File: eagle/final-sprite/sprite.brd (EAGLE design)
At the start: 35 x 35 mm, 40 parts

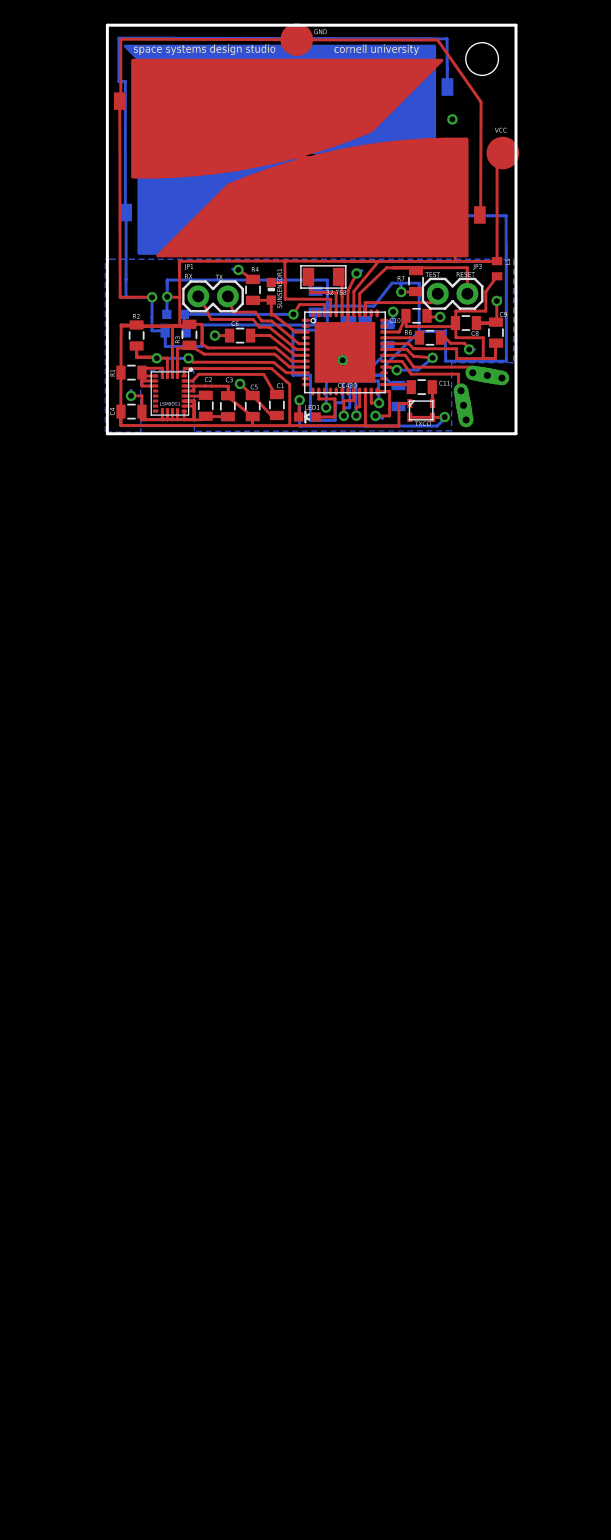
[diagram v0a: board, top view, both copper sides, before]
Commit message: merged final-sprite changes into master branch
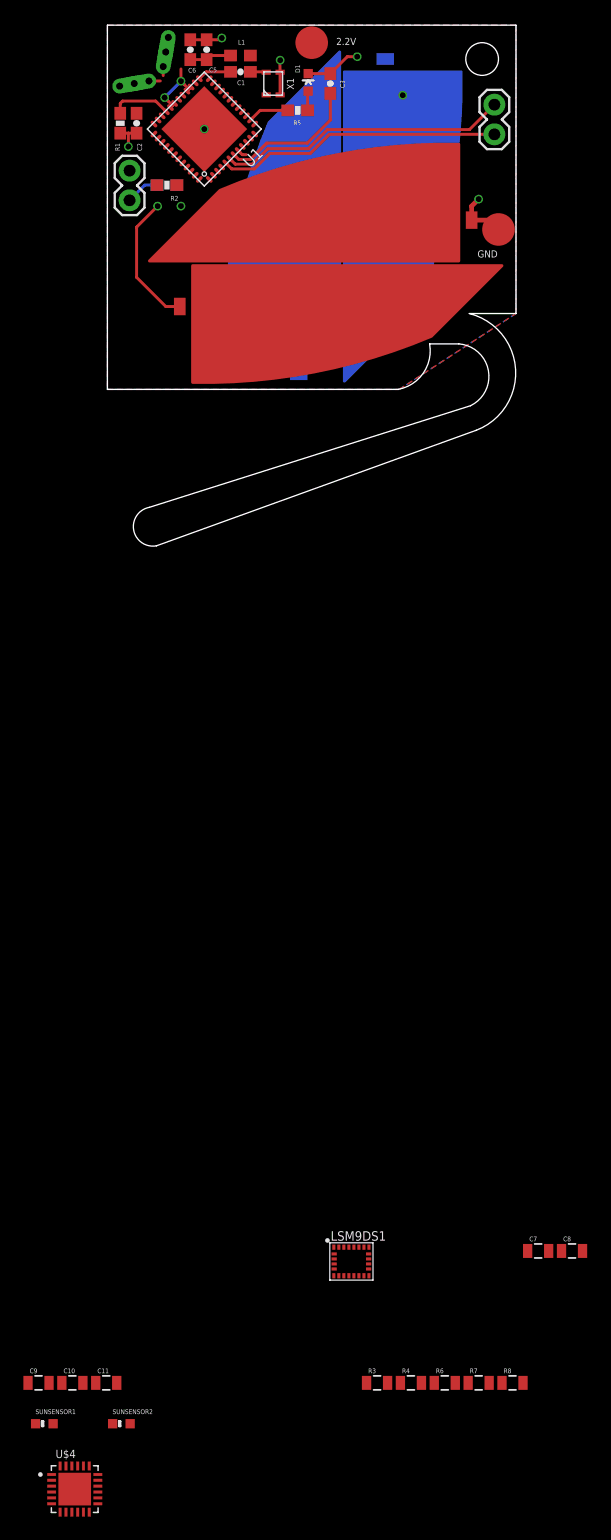
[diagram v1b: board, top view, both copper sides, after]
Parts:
- removed 32KHZ: SPRITECRYSTALSPRITECRYSTAL, SpriteCrystal:SPRITECRYSTAL
- removed ANTENNA1, ANTENNA2: ANTENNA, SpriteAntenna:ANTENNA
- removed C12: 10uF, SparkFun:0805
- removed CC430: CC430F513X---RGZ48, TI_MSP430_v16:RGZ48
- removed GNDPIN, VCCPIN: SPRITE_PIN, SpritePin:SPRITE_PIN
- removed H-BRIDGE: LV8417CS, lv8417cs:LV8417CS
- removed JP1: (no value), SparkFun:1X02
- removed LED1: (no value), SparkFun:LED-0603
- removed RECTIFIER: NSR1030QMUTAG, NSR1030QMUTAG:NSR1030QMUTAG
- removed TRISOL1, TRISOL2, TRISOL3, TRISOL4: TRISOLX-WING, TriSolX_QzQube:TRISOLX-T01
- removed TXCO: (no value), SpriteTCXO:TXC_7Z
- added ANT-N, ANT-P: ANTENNA, SpriteAntenna:ANTENNA
- added D1: (no value), SparkFun:LED-0603
- added JP2: (no value), SparkFun:1X02
- added P1, P2: SPRITE_PIN, SpritePin:SPRITE_PIN
- added S1, S2, S3, S4: TRISOLX-WING, TriSolX_QzQube:TRISOLX-T01
- added U$1: UMAC, UMAC:UMAC
- added U$4: ADP5092, STAC:QFN50P400X400X100-25N
- added U1: CC430F5137, TI_MSP430_v16:RGZ48
- added X1: TCXO_7Z, SpriteTCXO:TXC_7Z
- C1: value 0.1uF -> 10 nF; device SparkFun:0805 -> SparkFun:0603-CAP
- C10: value 470nF -> 0.1uF
- C11: value 10nF -> 10uF
- C2: value 10nF -> 470nF; device SparkFun:0805 -> SparkFun:0603-CAP
- C3: value 0.1uF -> 470nF; device SparkFun:0805 -> SparkFun:0603-CAP
- C4: value 0.1uF -> 2.2nF; device SparkFun:0805 -> SparkFun:0603-CAP
- C5: value 10uF -> 10nF; device SparkFun:0805 -> SparkFun:0603-CAP
- C6: value 470nF -> 100nF; device SparkFun:0805 -> SparkFun:0603-CAP
- C7: value 10uF -> 0.1uF
- L1: value 12nH -> 12 nH; device SparkFun:C0402 -> SparkFun:0603
- R1: value 10K -> 56K; device SparkFun:0805 -> SparkFun:0603-RES
- R2: value 10K -> 47K; device SparkFun:0805 -> SparkFun:0603-RES
- R5: value 10K -> 270R; device SparkFun:0805 -> SparkFun:0603-RES
- R6, R7: value 56K -> 10K
- R8: value 1K -> 10K
- moved SUNSENSOR1 98.9 mm to (-5.40, -84.8), turned to 0 degrees
- moved C9 98.1 mm to (-5.90, -81.3), turned to 0 degrees
- moved C10 96.0 mm to (-3.00, -81.3)
- moved SUNSENSOR2 95.1 mm to (1.20, -84.8), flipped to the top, turned to 0 degrees
- moved R4 94.6 mm to (26.0, -81.3), turned to 0 degrees
- moved R7 94.5 mm to (31.8, -81.3), turned to 0 degrees
- moved R3 91.2 mm to (23.1, -81.3), turned to 0 degrees
- moved R8 90.4 mm to (34.7, -81.3), flipped to the top, turned to 0 degrees
- moved R6 89.5 mm to (28.9, -81.3), turned to 0 degrees
- moved C11 89.5 mm to (-0.10, -81.3)
- moved C7 83.5 mm to (36.9, -70.0), flipped to the top, turned to 0 degrees
- moved C8 80.0 mm to (39.8, -70.0)
- moved LSM9DS1 76.0 mm to (20.9, -70.9), turned to 0 degrees
- moved C5 30.8 mm to (8.50, 32.9)
- moved C3 29.0 mm to (19.1, 30.0), turned to 90 degrees
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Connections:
- removed net #RST/SBWTDIO: CC430.40, JP3.1, R7.2
- removed net ANT1: ANTENNA1.IN1, ANTENNA1.IN2, ANTENNA1.IN3, CC430.29
- removed net ANT2: ANTENNA2.IN1, ANTENNA2.IN2, ANTENNA2.IN3, CC430.30
- removed net COIL1: H-BRIDGE.OUT1, R8.1, RECTIFIER.PIN1
- removed net GUARD: C10.1, C8.1, C9.1, CC430.27, CC430.28, CC430.31, CC430.32, CC430.34, L1.2
- removed net LOADLINE: H-BRIDGE.OUT2, R8.2, RECTIFIER.PIN3
- removed net N$8: 32KHZ.PIN1, CC430.43
- removed net P1.0: CC430.13
- removed net P1.1: CC430.12
- removed net P1.2: CC430.11
- removed net P1.7: CC430.4
- removed net P2.1/A1: CC430.2
- removed net P2.2/A2: CC430.1
- removed net P2.2/A4: CC430.47
- removed net P2.3/A3: CC430.48
- removed net P2.6: CC430.24
- removed net P2.7: CC430.23, H-BRIDGE.IN2
- removed net P3.0: CC430.21, H-BRIDGE.IN1
- removed net P3.1: CC430.20, H-BRIDGE.ENA
- removed net P3.2: CC430.19
- removed net P3.3: CC430.18
- removed net P3.4: CC430.17
- removed net P3.5: CC430.16
- removed net P3.6: CC430.15
- removed net P3.7: CC430.14, LED1.A
- removed net R_BIAS: CC430.33, R6.2
- removed net TCK_PJ.3: CC430.38
- removed net TDI_PJ.1: CC430.36
- removed net TDO_PJ.0: CC430.35
- removed net TEST/SBWTCK: CC430.39, JP3.2
- removed net TMS_PJ.2: CC430.37
- removed net VCORE: C6.2, CC430.7
- new net N$11: D1.A, R5.1
- new net N$12: C1.2, X1.OUT
- new net N$6: C8.1, LSM9DS1.21
- new net PGOOD: U$4.19
- new net REGGOOD: U$4.11
- new net RF_N: ANT-N.IN1, ANT-N.IN2, ANT-N.IN3, U1.30
- new net RF_P: ANT-P.IN1, ANT-P.IN2, ANT-P.IN3, U1.29
- new net RST: C4.2, JP2.1, R2.1, U1.40
- new net TST: JP2.2, U1.39
- new net VBAT: U$1.V+, U$4.17
- new net VCCA: C5.1, C6.1, L1.2, U1.27, U1.28, U1.31, U1.32
- new net VCCINT: S1.P$2, S2.P$2, S3.P$2, S4.P$2
- new net VCCIO: U$4.14, U$4.15
- net GND: now also C11.2, C4.1, C6.2, C7.2, D1.C, P2.PIN, R1.2, R7.1, R8.1, S1.P$3, S2.P$3, S3.P$3, S4.P$3, U$1.V-, U$4.12, U$4.25, U$4.7, U1.42, U1.TP, X1.GND1, X1.GND2; no longer C1.2, C12.1, C4.2, C6.1, C7.1, CC430.42, CC430.TP, GNDPIN.PIN, H-BRIDGE.PGND, H-BRIDGE.SGND, LED1.C, R4.1, R5.1, R6.1, RECTIFIER.GND, TRISOL1.P$3, TRISOL2.P$3, TRISOL3.P$3, TRISOL4.P$3, TXCO.GND1, TXCO.GND2
- net N$1: now also U1.25; no longer LSM9DS1.24
- net N$2: now also R5.2, U1.14; no longer C2.1, LSM9DS1.21
- net N$3: now also U1.33; no longer LSM9DS1.5, LSM9DS1.6, LSM9DS1.7, LSM9DS1.8
- net N$4: now also C3.1, U1.7; no longer C11.1, CC430.25
- net N$5: now also C7.1, LSM9DS1.24; no longer C11.2, TXCO.OUT
- net N$7: now also LSM9DS1.5, LSM9DS1.6, LSM9DS1.7, LSM9DS1.8, R3.1; no longer 32KHZ.PIN2, CC430.44
- net P2.0/A0: now also R7.2; no longer CC430.3, R4.2
- net P2.5/A5: now also R8.2; no longer CC430.46, R5.2
- net SCL: now also R6.1, U1.9; no longer CC430.9, R3.1
- net SDA: now also R4.1, U1.10; no longer CC430.10, R2.1
- net UART_RX: now also JP3.2, U1.6; no longer CC430.6, JP1.2
- net UART_TX: now also JP3.1, U1.5; no longer CC430.5, JP1.1
- net VCC: now also C10.1, C11.1, C2.1, C9.1, P1.PIN, R4.2, R6.2, U$4.16, U1.22, U1.34, U1.41, U1.45, U1.8, X1.VCC; no longer C12.2, C3.1, C4.1, C5.1, C7.2, CC430.22, CC430.41, CC430.45, CC430.8, H-BRIDGE.VCC, H-BRIDGE.VM, R1.2, R7.1, RECTIFIER.VCC, TRISOL1.P$2, TRISOL2.P$2, TRISOL3.P$2, TRISOL4.P$2, TXCO.VCC, VCCPIN.PIN
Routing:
- net COIL1: track 1132.3 -> 0.00 mm, vias 3 -> 0
- net VCC: track 371.4 -> 0.85 mm, vias 2 -> 0
- net GND: track 226.3 -> 29.9 mm, vias 12 -> 6
- net GUARD: track 44.1 -> 0.00 mm, vias 2 -> 0
- net VCCINT: track 0.00 -> 23.3 mm, vias 0 -> 1
- net SDA: track 21.1 -> 0.00 mm, vias 2 -> 0
- net #RST/SBWTDIO: track 16.1 -> 0.00 mm
- net UART_TX: track 8.73 -> 24.5 mm
- net P2.5/A5: track 14.7 -> 0.00 mm, vias 1 -> 0
- net SCL: track 14.6 -> 0.00 mm
- net UART_RX: track 11.6 -> 25.0 mm
- net ANT1: track 11.2 -> 0.00 mm
- net ANT2: track 11.1 -> 0.00 mm
- net VCCA: track 0.00 -> 9.55 mm, vias 0 -> 2
- net N$4: track 2.55 -> 12.1 mm
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- added copper zone on layer 1, net VCC
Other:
- board size 35 x 35 mm -> 35 x 44.6 mm
- board text added: "2.2V"
- board text added: "Sprite v2.6"
- board text removed: "RESET"
- board text removed: "RX"
- board text removed: "TEST"
- board text removed: "TX"
- board text removed: "VCC"
- board text removed: "cornell university"
- board text removed: "space systems design studio"

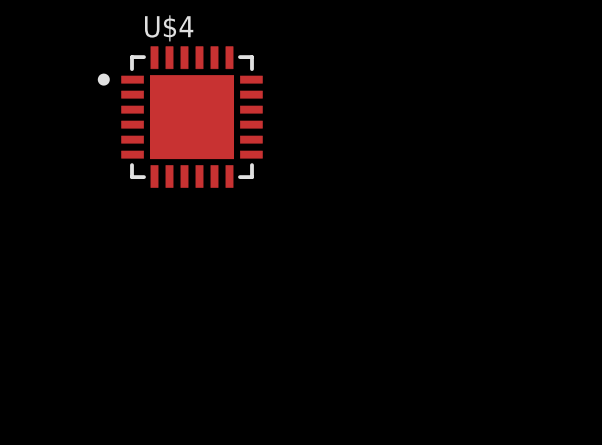
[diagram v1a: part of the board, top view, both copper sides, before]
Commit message: Add DRV8833CRTER
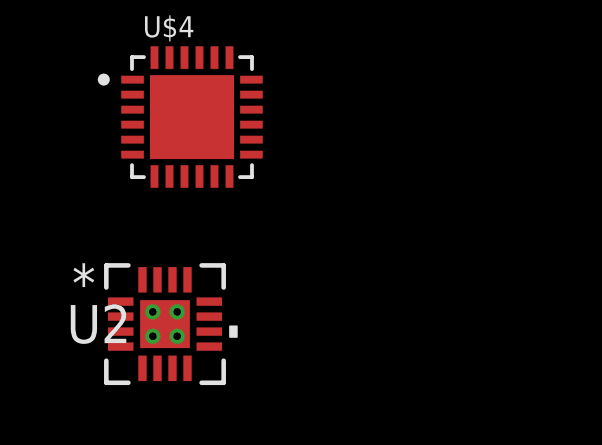
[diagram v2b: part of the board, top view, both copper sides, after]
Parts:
- added U2: DRV8833CRTER, STAC:RTE16_1P66X1P66
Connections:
- new net VM: U2.10
- net GND: now also U2.11
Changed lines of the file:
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@@
 <?xml version="1.0" encoding="utf-8"?>
 <!DOCTYPE eagle SYSTEM "eagle.dtd">
-<eagle version="9.0.1">
+<eagle version="9.0.0">
 <drawing>
 <settings>
@@
 <element name="R8" library="SparkFun" package="0805" value="10K" x="34.7" y="-81.3"/>
 <element name="U$4" library="STAC" package="QFN50P400X400X100-25N" value="ADP5092" x="-2.8" y="-90.4"/>
+<element name="U2" library="STAC" package="RTE16_1P66X1P66" value="DRV8833CRTER" x="-3.7" y="-97.3">
+<attribute name="AUTHOR" value="Ultra-Librarian" x="-3.7" y="-97.3" size="1.778" layer="27" display="off"/>
+<attribute name="CHECKED" value="Kevin Zheng" x="-3.7" y="-97.3" size="1.778" layer="27" display="off"/>
+<attribute name="DIGI-KEY_PN" value="296-40079-1-ND" x="-3.7" y="-97.3" size="1.778" layer="27" display="off"/>
+<attribute name="MANUFACTURER_PART_NUMBER" value="DRV8833CRTER" x="-3.7" y="-97.3" size="1.778" layer="27" display="off"/>
+<attribute name="VENDOR" value="Texas Instruments" x="-3.7" y="-97.3" size="1.778" layer="27" display="off"/>
+</element>
 </elements>
 <signals>
@@
 <contactref element="U$4" pad="12"/>
 <contactref element="U$4" pad="25"/>
-<wire x1="-2.8" y1="-90.4" x2="-4.05" y2="-92.38" width="0" layer="19" extent="1-1"/>
-<wire x1="-1.55" y1="-92.38" x2="-2.8" y2="-90.4" width="0" layer="19" extent="1-1"/>
+<contactref element="U2" pad="11"/>
+<wire x1="-1.55" y1="-92.38" x2="-2.225" y2="-97.05" width="0" layer="19" extent="1-1"/>
+<wire x1="-2.8" y1="-90.4" x2="-1.55" y2="-92.38" width="0" layer="19" extent="1-1"/>
+<wire x1="-4.05" y1="-92.38" x2="-2.8" y2="-90.4" width="0" layer="19" extent="1-1"/>
 <wire x1="-2.1" y1="-81.3" x2="-2.8" y2="-90.4" width="0" layer="19" extent="1-1"/>
 <wire x1="-5" y1="-81.3" x2="-2.1" y2="-81.3" width="0" layer="19" extent="1-1"/>
@@
 <wire x1="-0.82" y1="-90.65" x2="-0.82" y2="-91.15" width="0" layer="19" extent="1-1"/>
 </signal>
+<signal name="VM">
+<contactref element="U2" pad="10"/>
+</signal>
 </signals>

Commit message: Place COIL?_IN? pins
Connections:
- new net COIL1_IN1: U1.20
- new net COIL1_IN2: U1.19
- new net COIL2_IN1: U1.18
- new net COIL2_IN2: U1.17
- new net COIL3_IN1: U1.2
- new net COIL3_IN2: U1.1
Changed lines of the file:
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@@
 <contactref element="U2" pad="10"/>
+</signal>
+<signal name="COIL1_IN1">
+<contactref element="U1" pad="20"/>
+</signal>
+<signal name="COIL1_IN2">
+<contactref element="U1" pad="19"/>
+</signal>
+<signal name="COIL2_IN1">
+<contactref element="U1" pad="18"/>
+</signal>
+<signal name="COIL2_IN2">
+<contactref element="U1" pad="17"/>
+</signal>
+<signal name="COIL3_IN1">
+<contactref element="U1" pad="2"/>
+</signal>
+<signal name="COIL3_IN2">
+<contactref element="U1" pad="1"/>
 </signal>
 </signals>

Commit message: More progress on COIL12
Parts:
- added C12: 10uF, SparkFun:0603-CAP
- added C13: 2.2uF, SparkFun:0603-CAP
- added R10, R9: 270R, SparkFun:0603-RES
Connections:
- removed net VM: U2.10
- new net COIL12_EN: U1.16, U2.15
- new net COIL12_FAULT: U1.13, U2.6
- new net COIL3_EN: U1.48
- new net COIL3_FAULT: U1.12
- new net N$10: R10.2, U2.1
- new net N$8: C13.1, U2.12
- new net N$9: R9.2, U2.4
- net COIL1_IN1: now also U2.14
- net COIL1_IN2: now also U2.13
- net COIL2_IN1: now also U2.7
- net COIL2_IN2: now also U2.8
- net GND: now also C12.2, C13.2, R10.1, R9.1, U2.17
- net VCCIO: now also C12.1, U2.10
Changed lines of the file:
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@@
 <attribute name="VENDOR" value="Texas Instruments" x="-3.7" y="-97.3" size="1.778" layer="27" display="off"/>
 </element>
+<element name="C12" library="SparkFun" package="0603-CAP" value="10uF" x="-4.8" y="-101.6"/>
+<element name="C13" library="SparkFun" package="0603-CAP" value="2.2uF" x="-4.8" y="-104.6"/>
+<element name="R9" library="SparkFun" package="0603-RES" value="270R" x="-4.8" y="-107.6"/>
+<element name="R10" library="SparkFun" package="0603-RES" value="270R" x="-4.8" y="-110.6"/>
 </elements>
 <signals>
@@
 <contactref element="U$4" pad="25"/>
 <contactref element="U2" pad="11"/>
+<contactref element="U2" pad="17"/>
+<contactref element="C12" pad="2"/>
+<contactref element="C13" pad="2"/>
+<contactref element="R9" pad="1"/>
+<contactref element="R10" pad="1"/>
+<wire x1="-5.65" y1="-107.6" x2="-5.65" y2="-110.6" width="0" layer="19" extent="1-1"/>
+<wire x1="-3.95" y1="-104.6" x2="-5.65" y2="-107.6" width="0" layer="19" extent="1-1"/>
+<wire x1="-3.95" y1="-101.6" x2="-3.95" y2="-104.6" width="0" layer="19" extent="1-1"/>
+<wire x1="-3.7" y1="-97.3" x2="-3.95" y2="-101.6" width="0" layer="19" extent="1-1"/>
+<wire x1="-2.225" y1="-97.05" x2="-3.7" y2="-97.3" width="0" layer="19" extent="1-1"/>
 <wire x1="-1.55" y1="-92.38" x2="-2.225" y2="-97.05" width="0" layer="19" extent="1-1"/>
 <wire x1="-2.8" y1="-90.4" x2="-1.55" y2="-92.38" width="0" layer="19" extent="1-1"/>
@@
 <contactref element="U$4" pad="14"/>
 <contactref element="U$4" pad="15"/>
+<contactref element="C12" pad="1"/>
+<contactref element="U2" pad="10"/>
+<wire x1="-2.225" y1="-97.55" x2="-5.65" y2="-101.6" width="0" layer="19" extent="1-1"/>
+<wire x1="-0.82" y1="-91.15" x2="-2.225" y2="-97.55" width="0" layer="19" extent="1-1"/>
 <wire x1="-0.82" y1="-90.65" x2="-0.82" y2="-91.15" width="0" layer="19" extent="1-1"/>
-</signal>
-<signal name="VM">
-<contactref element="U2" pad="10"/>
 </signal>
 <signal name="COIL1_IN1">
 <contactref element="U1" pad="20"/>
+<contactref element="U2" pad="14"/>
+<wire x1="10.138475" y1="28.9991375" x2="-3.4499375" y2="-95.825" width="0" layer="19" extent="1-1"/>
 </signal>
 <signal name="COIL1_IN2">
 <contactref element="U1" pad="19"/>
+<contactref element="U2" pad="13"/>
+<wire x1="10.492028125" y1="28.645584375" x2="-2.9498125" y2="-95.825" width="0" layer="19" extent="1-1"/>
 </signal>
 <signal name="COIL2_IN1">
 <contactref element="U1" pad="18"/>
+<contactref element="U2" pad="7"/>
+<wire x1="10.845584375" y1="28.292028125" x2="-3.4499375" y2="-98.775" width="0" layer="19" extent="1-1"/>
 </signal>
 <signal name="COIL2_IN2">
 <contactref element="U1" pad="17"/>
+<contactref element="U2" pad="8"/>
+<wire x1="11.1991375" y1="27.938475" x2="-2.9498125" y2="-98.775" width="0" layer="19" extent="1-1"/>
 </signal>
 <signal name="COIL3_IN1">
@@
 <contactref element="U1" pad="1"/>
 </signal>
+<signal name="N$8">
+<contactref element="C13" pad="1"/>
+<contactref element="U2" pad="12"/>
+<wire x1="-2.225" y1="-96.55" x2="-5.65" y2="-104.6" width="0" layer="19" extent="1-1"/>
+</signal>
+<signal name="COIL12_EN">
+<contactref element="U1" pad="16"/>
+<contactref element="U2" pad="15"/>
+<wire x1="11.552690625" y1="27.584921875" x2="-3.9500625" y2="-95.825" width="0" layer="19" extent="1-1"/>
+</signal>
+<signal name="COIL3_EN">
+<contactref element="U1" pad="48"/>
+</signal>
+<signal name="COIL12_FAULT">
+<contactref element="U1" pad="13"/>
+<contactref element="U2" pad="6"/>
+<wire x1="12.61335" y1="26.5242625" x2="-3.9500625" y2="-98.775" width="0" layer="19" extent="1-1"/>
+</signal>
+<signal name="COIL3_FAULT">
+<contactref element="U1" pad="12"/>
+</signal>
+<signal name="N$9">
+<contactref element="R9" pad="2"/>
+<contactref element="U2" pad="4"/>
+<wire x1="-5.175" y1="-98.05" x2="-3.95" y2="-107.6" width="0" layer="19" extent="1-1"/>
+</signal>
+<signal name="N$10">
+<contactref element="R10" pad="2"/>
+<contactref element="U2" pad="1"/>
+<wire x1="-5.175" y1="-96.55" x2="-3.95" y2="-110.6" width="0" layer="19" extent="1-1"/>
+</signal>
 </signals>

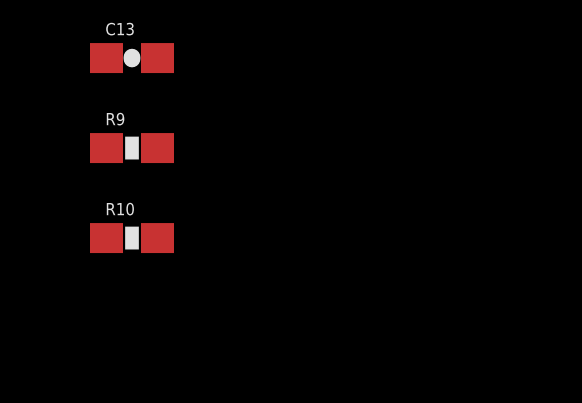
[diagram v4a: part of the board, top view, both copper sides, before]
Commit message: Complete one driver
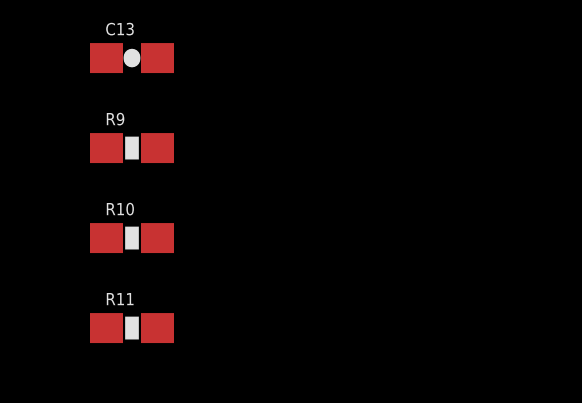
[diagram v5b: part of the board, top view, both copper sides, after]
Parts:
- added R11: 1K, SparkFun:0603-RES
- R10, R9: value 270R -> 15R
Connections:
- net COIL3_FAULT renamed COIL3_FAULT_B
- removed net COIL12_FAULT: U1.13, U2.6
- new net COIL12_FAULT_B: R11.1, U1.13, U2.6
- net VCC: now also R11.2
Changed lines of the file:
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@@
 <element name="C12" library="SparkFun" package="0603-CAP" value="10uF" x="-4.8" y="-101.6"/>
 <element name="C13" library="SparkFun" package="0603-CAP" value="2.2uF" x="-4.8" y="-104.6"/>
-<element name="R9" library="SparkFun" package="0603-RES" value="270R" x="-4.8" y="-107.6"/>
-<element name="R10" library="SparkFun" package="0603-RES" value="270R" x="-4.8" y="-110.6"/>
+<element name="R9" library="SparkFun" package="0603-RES" value="15R" x="-4.8" y="-107.6"/>
+<element name="R10" library="SparkFun" package="0603-RES" value="15R" x="-4.8" y="-110.6"/>
+<element name="R11" library="SparkFun" package="0603-RES" value="1K" x="-4.8" y="-113.6"/>
 </elements>
 <signals>
@@
 <contactref element="U1" pad="45"/>
 <contactref element="U$4" pad="16"/>
-<wire x1="-6.8" y1="-81.3" x2="-6.15" y2="-84.8" width="0" layer="19" extent="1-1"/>
-<wire x1="-3.9" y1="-81.3" x2="-6.8" y2="-81.3" width="0" layer="19" extent="1-1"/>
-<wire x1="-1" y1="-81.3" x2="-3.9" y2="-81.3" width="0" layer="19" extent="1-1"/>
-<wire x1="0.45" y1="-84.8" x2="-1" y2="-81.3" width="0" layer="19" extent="1-1"/>
-<wire x1="-0.82" y1="-90.15" x2="0.45" y2="-84.8" width="0" layer="19" extent="1-1"/>
+<contactref element="R11" pad="2"/>
+<wire x1="-0.82" y1="-90.15" x2="-3.95" y2="-113.6" width="0" layer="19" extent="1-1"/>
+<wire x1="0.45" y1="-84.8" x2="-0.82" y2="-90.15" width="0" layer="19" extent="1-1"/>
+<wire x1="-1" y1="-81.3" x2="0.45" y2="-84.8" width="0" layer="19" extent="1-1"/>
+<wire x1="-3.9" y1="-81.3" x2="-1" y2="-81.3" width="0" layer="19" extent="1-1"/>
+<wire x1="-6.8" y1="-81.3" x2="-3.9" y2="-81.3" width="0" layer="19" extent="1-1"/>
+<wire x1="-6.15" y1="-84.8" x2="-6.8" y2="-81.3" width="0" layer="19" extent="1-1"/>
 <wire x1="19.425" y1="-70.685" x2="-1" y2="-81.3" width="0" layer="19" extent="1-1"/>
 <wire x1="19.395" y1="-69.675" x2="19.425" y2="-70.685" width="0" layer="19" extent="1-1"/>
@@
 <contactref element="U1" pad="48"/>
 </signal>
-<signal name="COIL12_FAULT">
+<signal name="COIL12_FAULT_B">
 <contactref element="U1" pad="13"/>
 <contactref element="U2" pad="6"/>
+<contactref element="R11" pad="1"/>
+<wire x1="-3.9500625" y1="-98.775" x2="-5.65" y2="-113.6" width="0" layer="19" extent="1-1"/>
 <wire x1="12.61335" y1="26.5242625" x2="-3.9500625" y2="-98.775" width="0" layer="19" extent="1-1"/>
 </signal>
-<signal name="COIL3_FAULT">
+<signal name="COIL3_FAULT_B">
 <contactref element="U1" pad="12"/>
 </signal>
